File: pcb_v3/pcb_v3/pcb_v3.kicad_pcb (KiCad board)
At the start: 2 copper layers, 16 parts, among them J1 Conn_01x05_Socket, U10 TCRT5000, U11 TCRT5000, U3 NODEMCU-32S, U4 TCRT5000, U5 TCRT5000, U6 TCRT5000, U7 TCRT5000, U8 TCRT5000, U9 TCRT5000

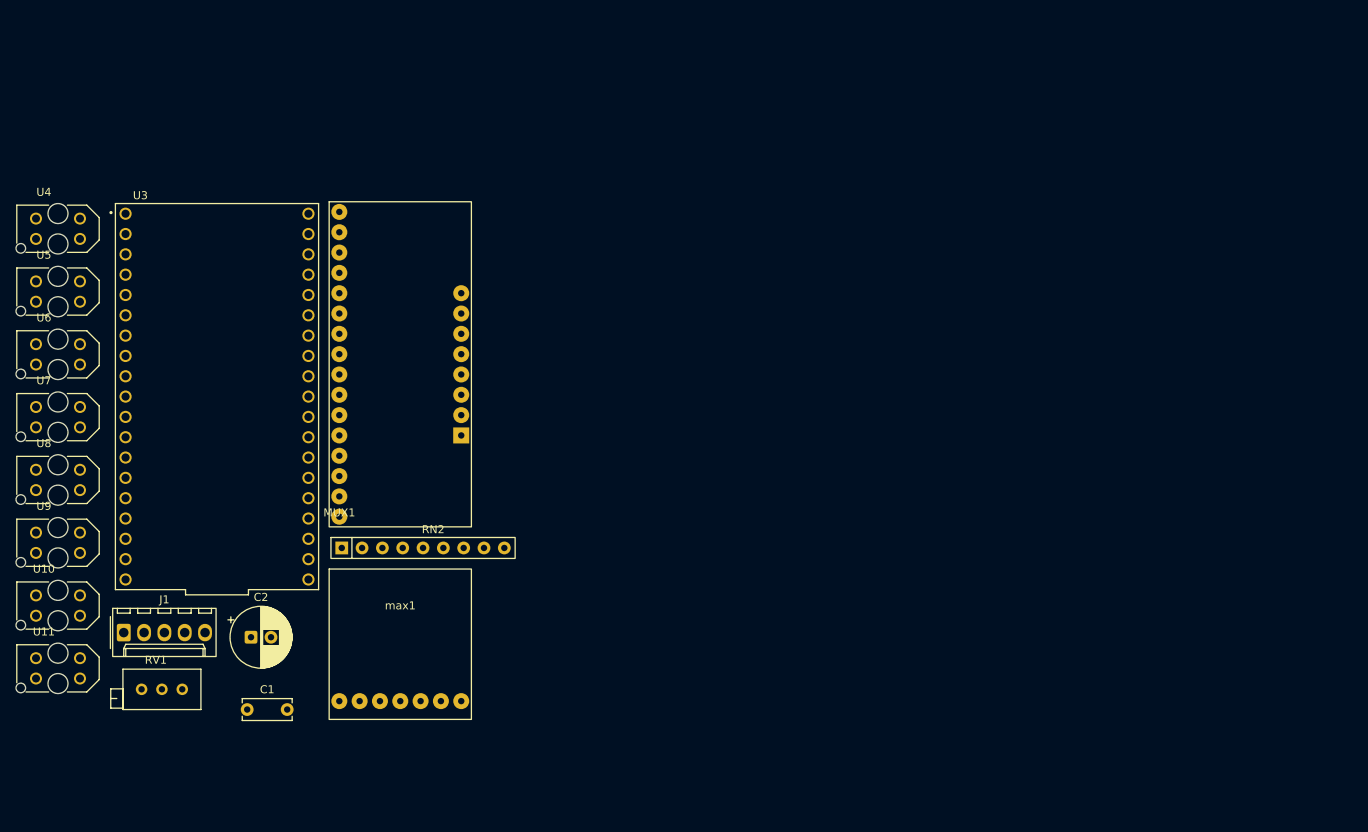
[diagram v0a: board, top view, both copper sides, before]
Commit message: wrong tcrt wiring
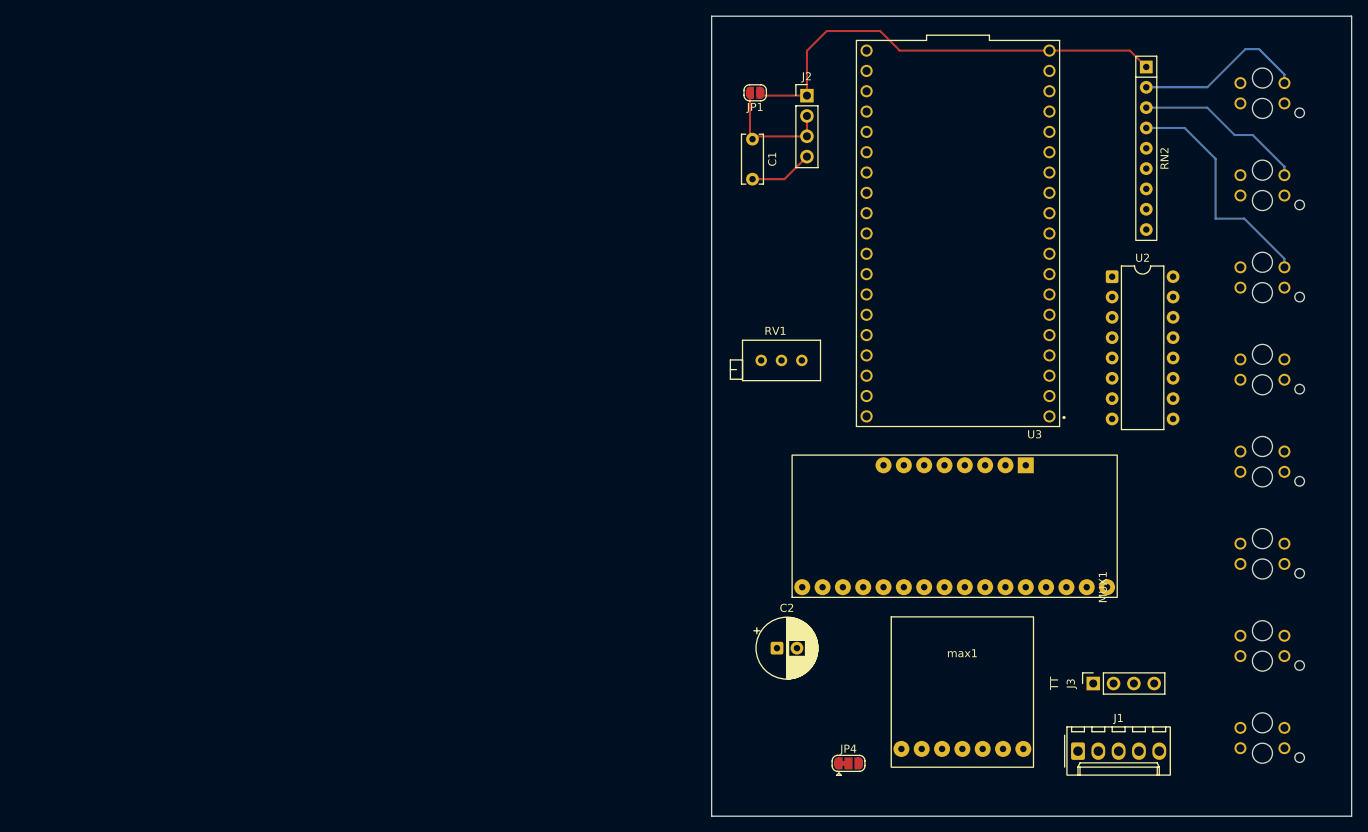
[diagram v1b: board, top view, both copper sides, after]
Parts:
- added J2: Conn_01x04_Pin, Connector_PinHeader_2.54mm:PinHeader_1x04_P2.54mm_Vertical, F.Cu at (164.5, 37.3)
- added J3: Conn_01x04_Socket, Connector_PinSocket_2.54mm:PinSocket_1x04_P2.54mm_Vertical, F.Cu at (200.3, 110.8)
- added JP1: SolderJumper_2_Open, Jumper:SolderJumper-2_P1.3mm_Open_RoundedPad1.0x1.5mm, F.Cu at (158.1, 36.9)
- added JP4: SolderJumper_3_Bridged12, Jumper:SolderJumper-3_P1.3mm_Bridged12_RoundedPad1.0x1.5mm, F.Cu at (169.7, 120.8)
- added U2: ULN2003A, Package_DIP:DIP-16_W7.62mm, F.Cu at (202.7, 59.9)
- U10, U11, U4, U5, U6, U7, U8, U9: moved to B.Cu
- moved U4 151.5 mm to (221.5, 37.0), turned to 180 degrees
- moved U8 151.2 mm to (221.5, 71.5), turned to 180 degrees
- moved U5 151.1 mm to (221.5, 48.5), turned to 180 degrees
- moved U6 150.9 mm to (221.5, 60.0), turned to 180 degrees
- moved U11 150.8 mm to (221.5, 117.6), turned to 180 degrees
- moved U7 150.7 mm to (221.5, 83.0), turned to 180 degrees
- moved U10 150.6 mm to (221.5, 106.1), turned to 180 degrees
- moved U9 150.6 mm to (221.5, 94.6), turned to 180 degrees
- moved J1 120.2 mm to (198.4, 119.2)
- moved RN2 117.2 mm to (207.0, 33.7), turned to -90 degrees
- moved MUX1 96.4 mm to (202.1, 98.7), turned to 90 degrees
- moved C1 95.2 mm to (157.7, 42.7), turned to -90 degrees
- moved U3 94.8 mm to (183.4, 54.5), turned to 180 degrees
- moved RV1 87.7 mm to (163.9, 70.4)
- moved max1 70.5 mm to (184.0, 107.5)
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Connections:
- U3 pad J2_13: unconnected-(U3-IO4-PadJ2_13) -> /TT_B
- U3 pad J2_15: unconnected-(U3-IO2-PadJ2_15) -> /TT_A
- max1 pad 4: unconnected-(max1-GAIN-Pad4) -> Net-(JP4-C)
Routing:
- net +5V: track 0.00 -> 56.9 mm
- net /R_U6: track 0.00 -> 29.5 mm
- net /R_U4: track 0.00 -> 21.6 mm
- net /R_U5: track 0.00 -> 21.4 mm
- net VCC: track 0.00 -> 15.4 mm
- net GND: track 0.00 -> 7.98 mm
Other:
- board outline added: 80 x 100 mm
- board text added: "TT"

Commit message: 1.delete useless pins in sch and layout 2.rewire potentiometer to vcc, enable us to modify voltage input for motor, preventing fast-battery run out. original wire(mux_sig) is now wired to 3.3v 3.pin9 on uln2003a is now wired to vcc, which previously wired to ground and cause short circuit 4.layout of 2pin power connecter is now modified to a 5mm spaceing module, let us connect power without any soldering on the wire of the battery socket --followings are suggest by seniors 5.jumper is now modify to _3_open , and useing a bigger pad ----todo 6.unify the size of pads on every holes 7.make the wire that crosses the motor socket to uln2003a wider
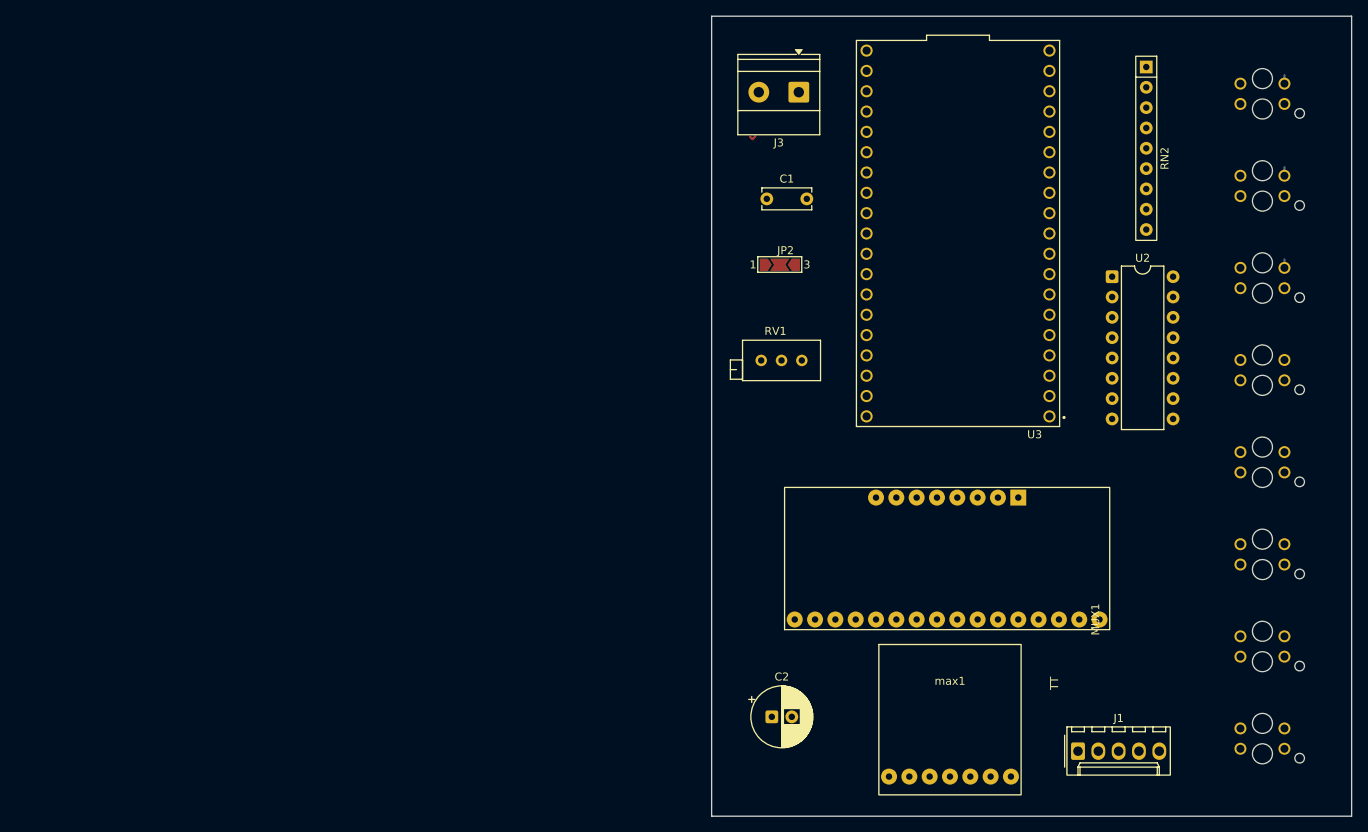
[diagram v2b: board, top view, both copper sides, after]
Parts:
- removed J2: Conn_01x04_Pin, Connector_PinHeader_2.54mm:PinHeader_1x04_P2.54mm_Vertical
- removed JP1: SolderJumper_2_Open, Jumper:SolderJumper-2_P1.3mm_Open_RoundedPad1.0x1.5mm
- removed JP4: SolderJumper_3_Bridged12, Jumper:SolderJumper-3_P1.3mm_Bridged12_RoundedPad1.0x1.5mm
- added JP2: SolderJumper_3_Open, Jumper:SolderJumper-3_P2.0mm_Open_TrianglePad1.0x1.5mm_NumberLabels, F.Cu at (161.1, 58.4)
- J3: footprint Connector_PinSocket_2.54mm:PinSocket_1x04_P2.54mm_Vertical -> TerminalBlock_Phoenix:TerminalBlock_Phoenix_MKDS-1,5-2_1x02_P5.00mm_Horizontal
- moved J3 82.6 mm to (163.5, 36.9), turned to 180 degrees
- moved C2 8.61 mm to (160.2, 114.9)
- moved C1 7.68 mm to (159.5, 50.2), turned to 0 degrees
- moved MUX1 4.15 mm to (201.1, 102.8)
- moved max1 3.79 mm to (182.4, 111.0)
- moved U8 0.07 mm to (221.5, 71.6)
- moved U4 0.07 mm to (221.5, 37.1)
- moved U5 0.07 mm to (221.5, 48.6)
- moved U6 0.07 mm to (221.5, 60.1)
- moved U10 0.07 mm to (221.5, 106.1)
- moved U11 0.07 mm to (221.5, 117.7)
- moved U7 0.07 mm to (221.5, 83.1)
- moved U9 0.07 mm to (221.5, 94.6)
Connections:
- J3 pad 1: /TT_A -> Net-(J3-Pin_1)
- J3 pad 2: /TT_B -> VCC
- RV1 pad 1: +3.3V -> GND
- RV1 pad 2: /MUX_SIG -> Net-(J3-Pin_1)
- U10 pad A: /U10_MUXc6 -> /R_U10
- U10 pad COLL: /R_U10 -> /U10_MUXc6
- U11 pad A: /U11_MUXc7 -> /R_U11
- U11 pad COLL: /R_U11 -> /U11_MUXc7
- U2 pad 9: GND -> VCC
- U3 pad J2_13: /TT_B -> unconnected-(U3-IO4-PadJ2_13)
- U3 pad J2_15: /TT_A -> unconnected-(U3-IO2-PadJ2_15)
- U4 pad A: /U4_MUXc0 -> /R_U4
- U4 pad COLL: /R_U4 -> /U4_MUXc0
- U5 pad A: /U5_MUXc1 -> /R_U5
- U5 pad COLL: /R_U5 -> /U5_MUXc1
- U6 pad A: /U6_MUXc2 -> /R_U6
- U6 pad COLL: /R_U6 -> /U6_MUXc2
- U7 pad A: /U7_MUXc3 -> /R_U7
- U7 pad COLL: /R_U7 -> /U7_MUXc3
- U8 pad A: /U8_MUXc4 -> /R_U8
- U8 pad COLL: /R_U8 -> /U8_MUXc4
- U9 pad A: /U9_MUXc5 -> /R_U9
- U9 pad COLL: /R_U9 -> /U9_MUXc5
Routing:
- net +5V: track 56.9 -> 0.00 mm
- net /R_U6: track 29.5 -> 0.00 mm
- net /R_U4: track 21.6 -> 0.00 mm
- net /R_U5: track 21.4 -> 0.00 mm
- net VCC: track 15.4 -> 0.95 mm
- net GND: track 7.98 -> 0.00 mm
- net /U4_MUXc0: track 0.00 -> 1.06 mm
- net /U6_MUXc2: track 0.00 -> 1.06 mm
- net /U5_MUXc1: track 0.00 -> 1.06 mm

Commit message: 1.linbf said tcrt Collector needs a 440ohm res., so i add a res. 2.i have modify the pads in the pcb to 1.95~2mm (depends on hole spaceing differences in diffierent footprints) and hole to 0.8mm
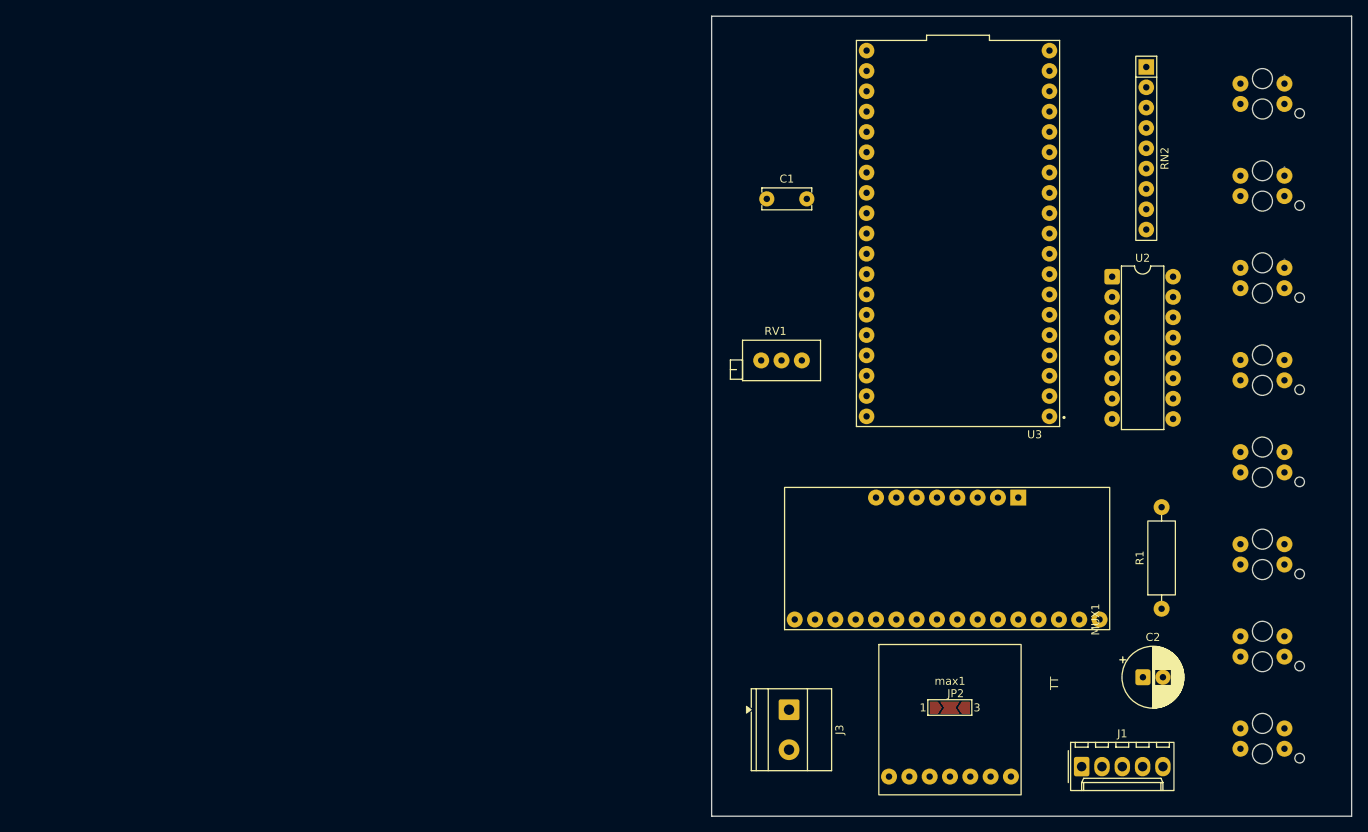
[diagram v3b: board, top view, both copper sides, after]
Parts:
- added R1: R, Resistor_THT:R_Axial_DIN0309_L9.0mm_D3.2mm_P12.70mm_Horizontal, F.Cu at (208.9, 101.4)
- moved J3 77.2 mm to (162.3, 114.0), turned to -90 degrees
- moved JP2 59.3 mm to (182.4, 113.8)
- moved C2 46.7 mm to (206.5, 110.0)
- moved J1 1.98 mm to (198.9, 121.2)
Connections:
- J3 pad 2: VCC -> GND
- RV1 pad 1: GND -> VCC
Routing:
- net VCC: track 0.95 -> 0.00 mm
